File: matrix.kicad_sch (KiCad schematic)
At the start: 42 parts, among them SW10 7/home, SW11 8/up, SW12 9/pgup, SW13 +, SW14 4/left, SW15 5, SW16 6/right, SW18 1/end, SW19 2/down, SW2 ESC, SW20 3/pgdn, SW22 0/insert, SW23 ./delete, SW24 ENTER, SW3 TAB, SW4 BACKSPACE, SW5 FN, SW6 NUM_LOCK, SW7 /, SW8 *, SW9 -

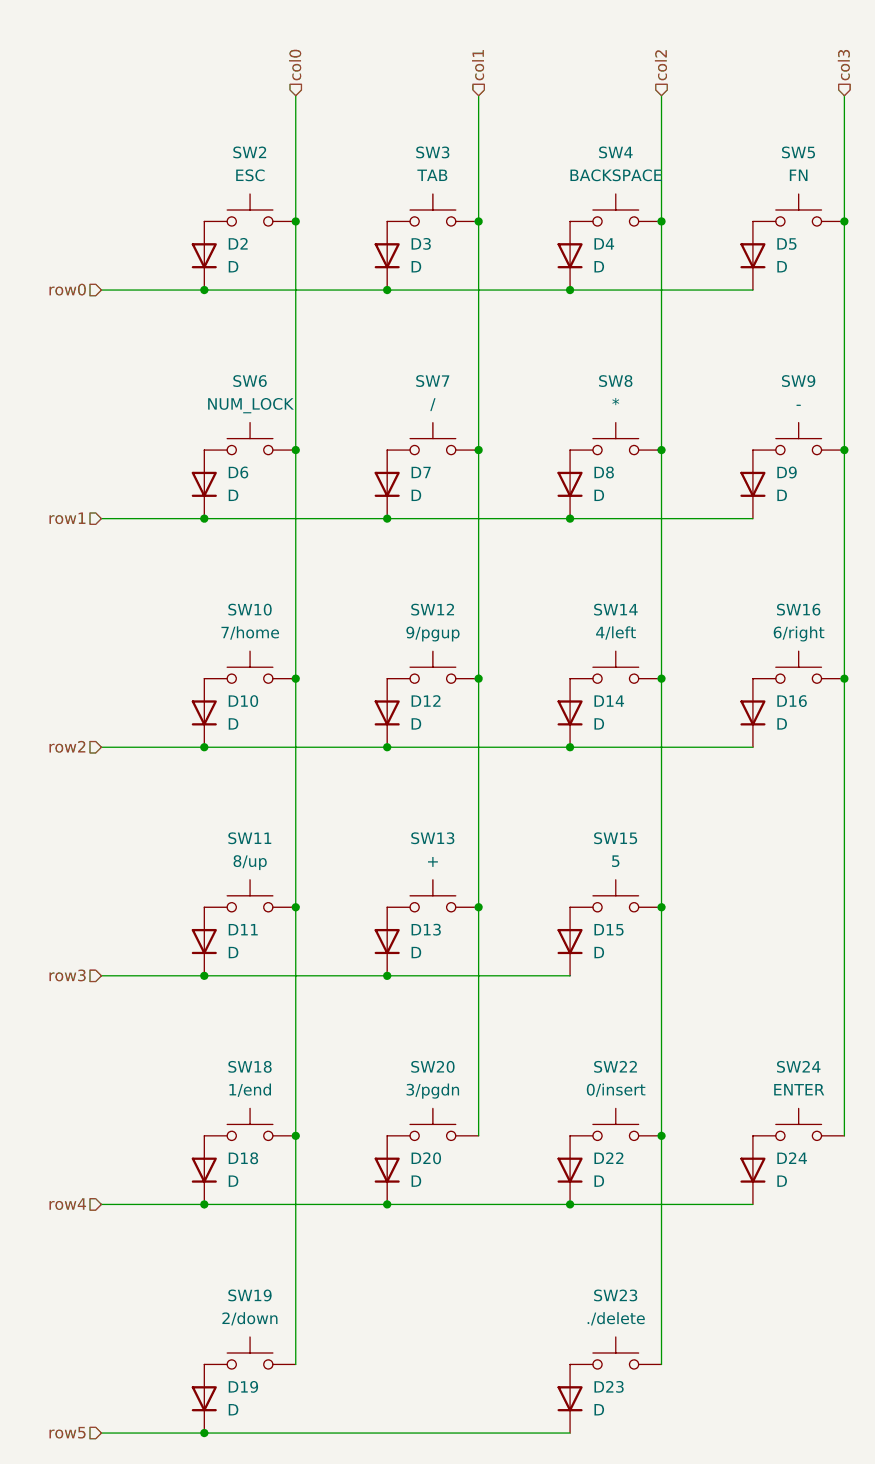
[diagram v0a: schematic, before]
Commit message: Fix schematic based on ERC
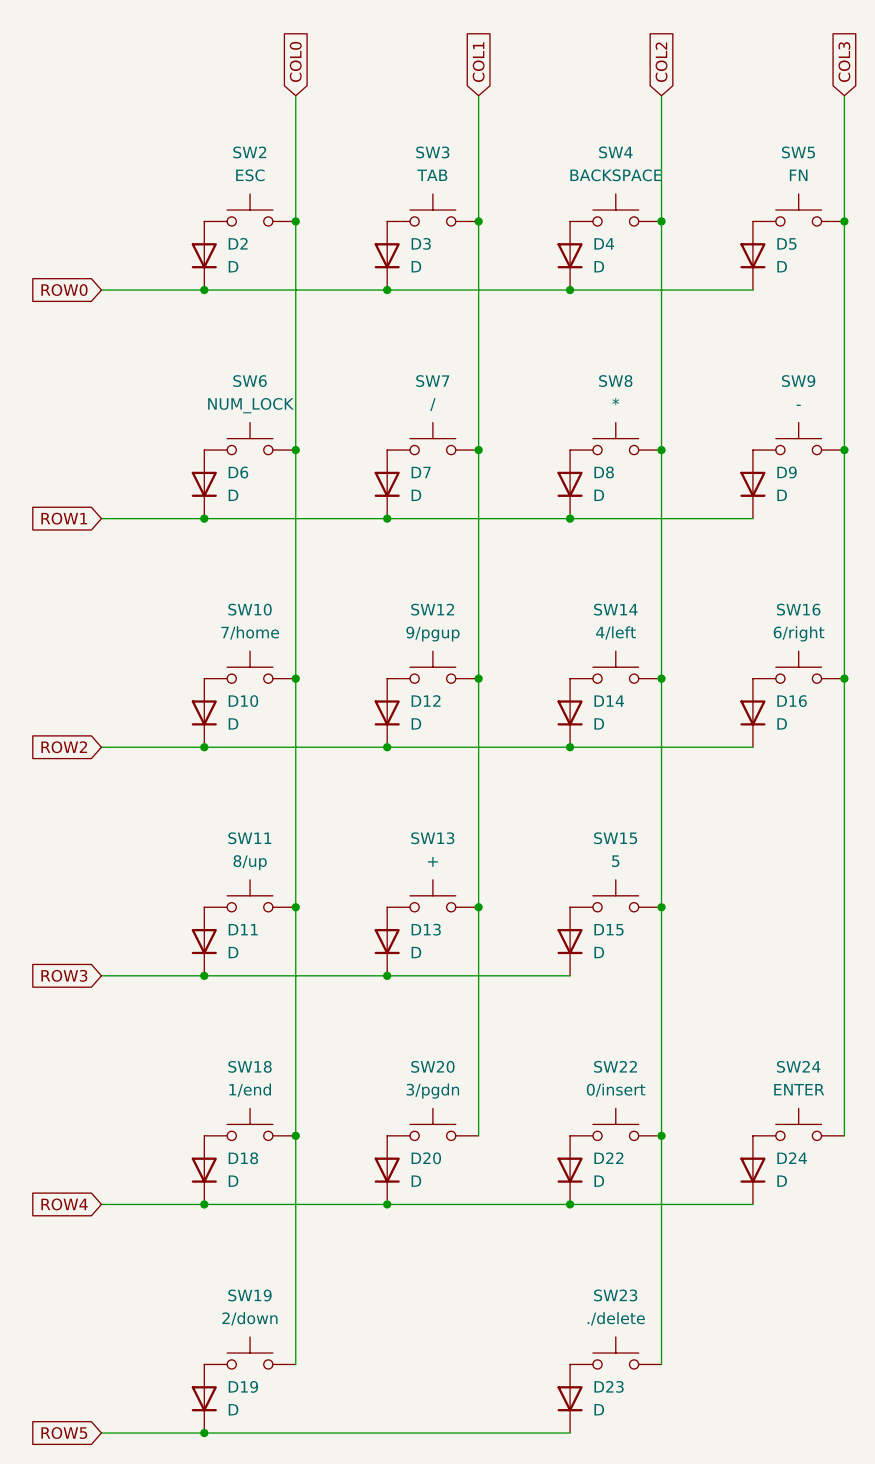
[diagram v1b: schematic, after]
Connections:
- net col0 renamed COL0
- net col1 renamed COL1
- net col2 renamed COL2
- net col3 renamed COL3
- net row0 renamed ROW0
- net row1 renamed ROW1
- net row2 renamed ROW2
- net row3 renamed ROW3
- net row4 renamed ROW4
- net row5 renamed ROW5
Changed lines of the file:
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@@
 		)
 	)
-	(hierarchical_label "row1"
+	(global_label "ROW0"
+		(shape input)
+		(at 57.15 49.53 180)
+		(fields_autoplaced yes)
+		(effects
+			(font
+				(size 1.27 1.27)
+			)
+			(justify right)
+		)
+		(property "Intersheetrefs" "${INTERSHEET_REFS}"
+			(at 48.9034 49.53 0)
+			(effects
+				(font
+					(size 1.27 1.27)
+				)
+				(justify right)
+				(hide yes)
+			)
+		)
+	)
+	(global_label "COL1"
+		(shape input)
+		(at 99.06 27.94 90)
+		(fields_autoplaced yes)
+		(effects
+			(font
+				(size 1.27 1.27)
+			)
+			(justify left)
+		)
+		(property "Intersheetrefs" "${INTERSHEET_REFS}"
+			(at 99.06 20.1167 90)
+			(effects
+				(font
+					(size 1.27 1.27)
+				)
+				(justify left)
+				(hide yes)
+			)
+		)
+	)
+	(global_label "ROW5"
+		(shape input)
+		(at 57.15 176.53 180)
+		(fields_autoplaced yes)
+		(effects
+			(font
+				(size 1.27 1.27)
+			)
+			(justify right)
+		)
+		(property "Intersheetrefs" "${INTERSHEET_REFS}"
+			(at 48.9034 176.53 0)
+			(effects
+				(font
+					(size 1.27 1.27)
+				)
+				(justify right)
+				(hide yes)
+			)
+		)
+	)
+	(global_label "ROW4"
+		(shape input)
+		(at 57.15 151.13 180)
+		(fields_autoplaced yes)
+		(effects
+			(font
+				(size 1.27 1.27)
+			)
+			(justify right)
+		)
+		(property "Intersheetrefs" "${INTERSHEET_REFS}"
+			(at 48.9034 151.13 0)
+			(effects
+				(font
+					(size 1.27 1.27)
+				)
+				(justify right)
+				(hide yes)
+			)
+		)
+	)
+	(global_label "ROW3"
+		(shape input)
+		(at 57.15 125.73 180)
+		(fields_autoplaced yes)
+		(effects
+			(font
+				(size 1.27 1.27)
+			)
+			(justify right)
+		)
+		(property "Intersheetrefs" "${INTERSHEET_REFS}"
+			(at 48.9034 125.73 0)
+			(effects
+				(font
+					(size 1.27 1.27)
+				)
+				(justify right)
+				(hide yes)
+			)
+		)
+	)
+	(global_label "ROW1"
 		(shape input)
 		(at 57.15 74.93 180)
-		(effects
-			(font
-				(size 1.27 1.27)
-			)
-			(justify right)
-		)
-	)
-	(hierarchical_label "row5"
-		(shape input)
-		(at 57.15 176.53 180)
-		(effects
-			(font
-				(size 1.27 1.27)
-			)
-			(justify right)
-		)
-	)
-	(hierarchical_label "row4"
-		(shape input)
-		(at 57.15 151.13 180)
-		(effects
-			(font
-				(size 1.27 1.27)
-			)
-			(justify right)
-		)
-	)
-	(hierarchical_label "row2"
+		(fields_autoplaced yes)
+		(effects
+			(font
+				(size 1.27 1.27)
+			)
+			(justify right)
+		)
+		(property "Intersheetrefs" "${INTERSHEET_REFS}"
+			(at 48.9034 74.93 0)
+			(effects
+				(font
+					(size 1.27 1.27)
+				)
+				(justify right)
+				(hide yes)
+			)
+		)
+	)
+	(global_label "ROW2"
 		(shape input)
 		(at 57.15 100.33 180)
-		(effects
-			(font
-				(size 1.27 1.27)
-			)
-			(justify right)
-		)
-	)
-	(hierarchical_label "col1"
-		(shape input)
-		(at 99.06 27.94 90)
-		(effects
-			(font
-				(size 1.27 1.27)
-			)
-			(justify left)
-		)
-	)
-	(hierarchical_label "col0"
+		(fields_autoplaced yes)
+		(effects
+			(font
+				(size 1.27 1.27)
+			)
+			(justify right)
+		)
+		(property "Intersheetrefs" "${INTERSHEET_REFS}"
+			(at 48.9034 100.33 0)
+			(effects
+				(font
+					(size 1.27 1.27)
+				)
+				(justify right)
+				(hide yes)
+			)
+		)
+	)
+	(global_label "COL0"
 		(shape input)
 		(at 78.74 27.94 90)
-		(effects
-			(font
-				(size 1.27 1.27)
-			)
-			(justify left)
-		)
-	)
-	(hierarchical_label "row3"
-		(shape input)
-		(at 57.15 125.73 180)
-		(effects
-			(font
-				(size 1.27 1.27)
-			)
-			(justify right)
-		)
-	)
-	(hierarchical_label "col2"
+		(fields_autoplaced yes)
+		(effects
+			(font
+				(size 1.27 1.27)
+			)
+			(justify left)
+		)
+		(property "Intersheetrefs" "${INTERSHEET_REFS}"
+			(at 78.74 20.1167 90)
+			(effects
+				(font
+					(size 1.27 1.27)
+				)
+				(justify left)
+				(hide yes)
+			)
+		)
+	)
+	(global_label "COL3"
+		(shape input)
+		(at 139.7 27.94 90)
+		(fields_autoplaced yes)
+		(effects
+			(font
+				(size 1.27 1.27)
+			)
+			(justify left)
+		)
+		(property "Intersheetrefs" "${INTERSHEET_REFS}"
+			(at 139.7 20.1167 90)
+			(effects
+				(font
+					(size 1.27 1.27)
+				)
+				(justify left)
+				(hide yes)
+			)
+		)
+	)
+	(global_label "COL2"
 		(shape input)
 		(at 119.38 27.94 90)
-		(effects
-			(font
-				(size 1.27 1.27)
-			)
-			(justify left)
-		)
-	)
-	(hierarchical_label "col3"
-		(shape input)
-		(at 139.7 27.94 90)
-		(effects
-			(font
-				(size 1.27 1.27)
-			)
-			(justify left)
-		)
-	)
-	(hierarchical_label "row0"
-		(shape input)
-		(at 57.15 49.53 180)
-		(effects
-			(font
-				(size 1.27 1.27)
-			)
-			(justify right)
-		)
-	)
+		(fields_autoplaced yes)
+		(effects
+			(font
+				(size 1.27 1.27)
+			)
+			(justify left)
+		)
+		(property "Intersheetrefs" "${INTERSHEET_REFS}"
+			(at 119.38 20.1167 90)
+			(effects
+				(font
+					(size 1.27 1.27)
+				)
+				(justify left)
+				(hide yes)
+			)
+		)
+	)

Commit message: Update PCB to show schematic changes
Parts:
- D10, D11, D12, D13, D14, D15, D16, D18, D19, D2, D20, D22, D23, D24, D3, D4, D5, D6, D7, D8, D9: footprint (none) -> Diode_SMD:D_SOD-123
- SW10, SW11, SW12, SW14, SW15, SW16, SW18, SW19, SW2, SW20, SW23, SW3, SW4, SW5, SW6, SW7, SW8, SW9: footprint (none) -> Alps_Only:ALPS-1U
- SW13, SW22, SW24: footprint (none) -> Alps_Only:ALPS-2U
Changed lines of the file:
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@@
 			)
 		)
-		(property "Footprint" ""
+		(property "Footprint" "Diode_SMD:D_SOD-123"
 			(at 129.54 96.52 0)
 			(effects
@@
 			)
 		)
-		(property "Footprint" ""
+		(property "Footprint" "Alps_Only:ALPS-1U"
 			(at 73.66 113.03 0)
 			(effects
@@
 			)
 		)
-		(property "Footprint" ""
+		(property "Footprint" "Diode_SMD:D_SOD-123"
 			(at 88.9 147.32 0)
 			(effects
@@
 			)
 		)
-		(property "Footprint" ""
+		(property "Footprint" "Alps_Only:ALPS-1U"
 			(at 93.98 138.43 0)
 			(effects
@@
 			)
 		)
-		(property "Footprint" ""
+		(property "Footprint" "Diode_SMD:D_SOD-123"
 			(at 88.9 45.72 0)
 			(effects
@@
 			)
 		)
-		(property "Footprint" ""
+		(property "Footprint" "Alps_Only:ALPS-1U"
 			(at 134.62 36.83 0)
 			(effects
@@
 			)
 		)
-		(property "Footprint" ""
+		(property "Footprint" "Diode_SMD:D_SOD-123"
 			(at 68.58 96.52 0)
 			(effects
@@
 			)
 		)
-		(property "Footprint" ""
+		(property "Footprint" "Diode_SMD:D_SOD-123"
 			(at 109.22 71.12 0)
 			(effects
@@
 			)
 		)
-		(property "Footprint" ""
+		(property "Footprint" "Diode_SMD:D_SOD-123"
 			(at 68.58 121.92 0)
 			(effects
@@
 			)
 		)
-		(property "Footprint" ""
+		(property "Footprint" "Diode_SMD:D_SOD-123"
 			(at 88.9 121.92 0)
 			(effects
@@
 			)
 		)
-		(property "Footprint" ""
+		(property "Footprint" "Alps_Only:ALPS-2U"
 			(at 134.62 138.43 0)
 			(effects
@@
 			)
 		)
-		(property "Footprint" ""
+		(property "Footprint" "Diode_SMD:D_SOD-123"
 			(at 129.54 147.32 0)
 			(effects
@@
 			)
 		)
-		(property "Footprint" ""
+		(property "Footprint" "Alps_Only:ALPS-1U"
 			(at 134.62 87.63 0)
 			(effects
@@
 			)
 		)
-		(property "Footprint" ""
+		(property "Footprint" "Diode_SMD:D_SOD-123"
 			(at 109.22 96.52 0)
 			(effects
@@
 			)
 		)
-		(property "Footprint" ""
+		(property "Footprint" "Alps_Only:ALPS-1U"
 			(at 93.98 87.63 0)
 			(effects
@@
 			)
 		)
-		(property "Footprint" ""
+		(property "Footprint" "Alps_Only:ALPS-1U"
 			(at 73.66 163.83 0)
 			(effects
@@
 			)
 		)
-		(property "Footprint" ""
+		(property "Footprint" "Alps_Only:ALPS-1U"
 			(at 73.66 62.23 0)
 			(effects
@@
 			)
 		)
-		(property "Footprint" ""
+		(property "Footprint" "Diode_SMD:D_SOD-123"
 			(at 109.22 121.92 0)
 			(effects
@@
 			)
 		)
-		(property "Footprint" ""
+		(property "Footprint" "Alps_Only:ALPS-2U"
 			(at 93.98 113.03 0)
 			(effects
@@
 			)
 		)
-		(property "Footprint" ""
+		(property "Footprint" "Diode_SMD:D_SOD-123"
 			(at 68.58 71.12 0)
 			(effects
@@
 			)
 		)
-		(property "Footprint" ""
+		(property "Footprint" "Alps_Only:ALPS-1U"
 			(at 73.66 138.43 0)
 			(effects
@@
 			)
 		)
-		(property "Footprint" ""
+		(property "Footprint" "Alps_Only:ALPS-1U"
 			(at 73.66 36.83 0)
 			(effects
@@
 			)
 		)
-		(property "Footprint" ""
+		(property "Footprint" "Alps_Only:ALPS-1U"
 			(at 93.98 62.23 0)
 			(effects
@@
 			)
 		)
-		(property "Footprint" ""
+		(property "Footprint" "Alps_Only:ALPS-1U"
 			(at 93.98 36.83 0)
 			(effects
@@
 			)
 		)
-		(property "Footprint" ""
+		(property "Footprint" "Alps_Only:ALPS-1U"
 			(at 114.3 163.83 0)
 			(effects
@@
 			)
 		)
-		(property "Footprint" ""
+		(property "Footprint" "Alps_Only:ALPS-1U"
 			(at 114.3 62.23 0)
 			(effects
@@
 			)
 		)
-		(property "Footprint" ""
+		(property "Footprint" "Diode_SMD:D_SOD-123"
 			(at 129.54 71.12 0)
 			(effects
@@
 			)
 		)
-		(property "Footprint" ""
+		(property "Footprint" "Alps_Only:ALPS-2U"
 			(at 114.3 138.43 0)
 			(effects
@@
 			)
 		)
-		(property "Footprint" ""
+		(property "Footprint" "Alps_Only:ALPS-1U"
 			(at 114.3 87.63 0)
 			(effects
@@
 			)
 		)
-		(property "Footprint" ""
+		(property "Footprint" "Diode_SMD:D_SOD-123"
 			(at 129.54 45.72 0)
 			(effects
@@
 			)
 		)
-		(property "Footprint" ""
+		(property "Footprint" "Diode_SMD:D_SOD-123"
 			(at 109.22 45.72 0)
 			(effects
@@
 			)
 		)
-		(property "Footprint" ""
+		(property "Footprint" "Diode_SMD:D_SOD-123"
 			(at 68.58 172.72 0)
 			(effects
@@
 			)
 		)
-		(property "Footprint" ""
+		(property "Footprint" "Diode_SMD:D_SOD-123"
 			(at 88.9 96.52 0)
 			(effects
@@
 			)
 		)
-		(property "Footprint" ""
+		(property "Footprint" "Diode_SMD:D_SOD-123"
 			(at 109.22 147.32 0)
 			(effects
@@
 			)
 		)
-		(property "Footprint" ""
+		(property "Footprint" "Diode_SMD:D_SOD-123"
 			(at 88.9 71.12 0)
 			(effects
@@
 			)
 		)
-		(property "Footprint" ""
+		(property "Footprint" "Alps_Only:ALPS-1U"
 			(at 73.66 87.63 0)
 			(effects
@@
 			)
 		)
-		(property "Footprint" ""
+		(property "Footprint" "Alps_Only:ALPS-1U"
 			(at 114.3 113.03 0)
 			(effects
@@
 			)
 		)
-		(property "Footprint" ""
+		(property "Footprint" "Diode_SMD:D_SOD-123"
 			(at 68.58 147.32 0)
 			(effects
@@
 			)
 		)
-		(property "Footprint" ""
+		(property "Footprint" "Alps_Only:ALPS-1U"
 			(at 134.62 62.23 0)
 			(effects
@@
 			)
 		)
-		(property "Footprint" ""
+		(property "Footprint" "Diode_SMD:D_SOD-123"
 			(at 68.58 45.72 0)
 			(effects
@@
 			)
 		)
-		(property "Footprint" ""
+		(property "Footprint" "Alps_Only:ALPS-1U"
 			(at 114.3 36.83 0)
 			(effects
@@
 			)
 		)
-		(property "Footprint" ""
+		(property "Footprint" "Diode_SMD:D_SOD-123"
 			(at 109.22 172.72 0)
 			(effects
